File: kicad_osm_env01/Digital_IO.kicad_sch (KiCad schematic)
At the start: 22 parts, among them U18 MIC94073YC6, U20 MIC94073YC6

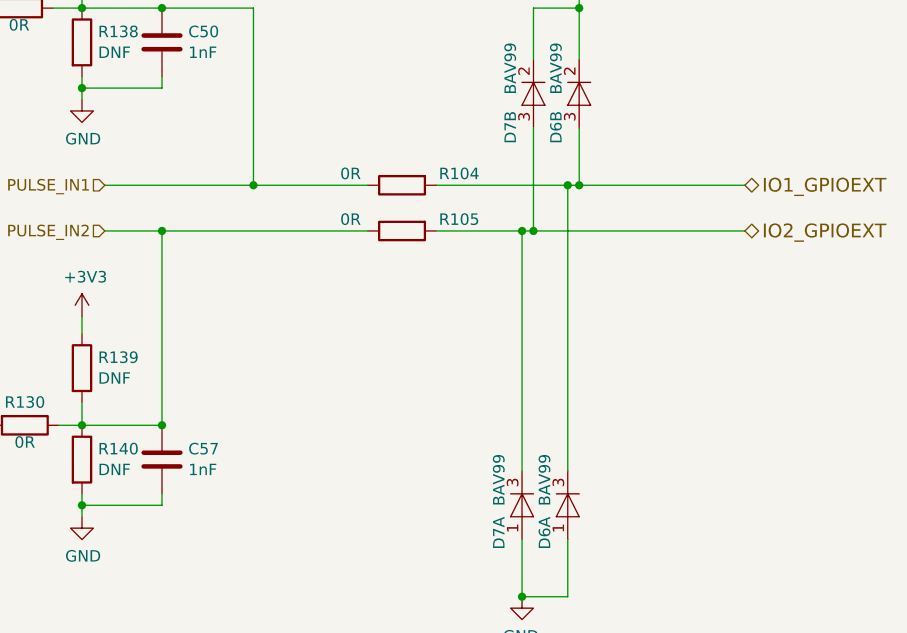
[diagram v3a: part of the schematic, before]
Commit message: updated schematics with 5V ored circuit and new 3v3 regulator
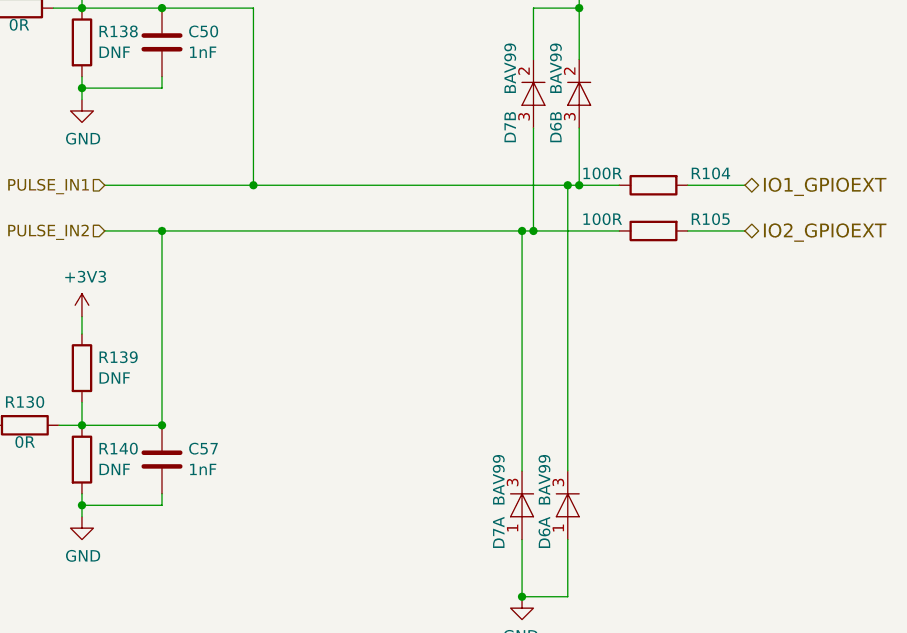
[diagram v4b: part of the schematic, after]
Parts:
- R104, R105: value 0R -> 100R
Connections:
- net IO1_GPIOEXT: no longer D6.3 (A), D6.3 (K)
- net IO2_GPIOEXT: no longer D7.3 (A), D7.3 (K)
- net PULSE_IN1: now also D6.3 (A), D6.3 (K)
- net PULSE_IN2: now also D7.3 (A), D7.3 (K)
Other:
- moved on the sheet: R104, R105
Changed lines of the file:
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@@
     (comment 1 "Part No: 304-010")
   )
+  (junction (at 208.915 85.09) (diameter 0) (color 0 0 0 0)
+  )
   (junction (at 92.71 65.405) (diameter 0) (color 0 0 0 0)
   )
@@
   (junction (at 154.94 120.65) (diameter 0) (color 0 0 0 0)
   )
+  (junction (at 205.105 90.17) (diameter 0) (color 0 0 0 0)
+  )
   (junction (at 203.835 90.17) (diameter 0) (color 0 0 0 0)
   )
@@
   (junction (at 93.345 111.76) (diameter 0) (color 0 0 0 0)
   )
-  (junction (at 205.105 90.17) (diameter 0) (color 0 0 0 0)
-  )
   (junction (at 120.65 148.59) (diameter 0) (color 0 0 0 0)
   )
+  (junction (at 210.185 85.09) (diameter 0) (color 0 0 0 0)
+  )
   (junction (at 154.94 65.405) (diameter 0) (color 0 0 0 0)
   )
@@
   (junction (at 154.94 111.76) (diameter 0) (color 0 0 0 0)
   )
-  (junction (at 208.915 85.09) (diameter 0) (color 0 0 0 0)
-  )
   (junction (at 173.99 85.09) (diameter 0) (color 0 0 0 0)
   )
   (junction (at 98.425 132.08) (diameter 0) (color 0 0 0 0)
   )
-  (junction (at 210.185 85.09) (diameter 0) (color 0 0 0 0)
-  )
   (junction (at 120.015 102.235) (diameter 0) (color 0 0 0 0)
   )
@@
     (stroke (width 0) (type default))
   )
-  (wire (pts (xy 173.99 85.09) (xy 186.69 85.09))
+  (wire (pts (xy 173.99 85.09) (xy 208.915 85.09))
     (stroke (width 0) (type default))
   )
@@
     (stroke (width 0) (type default))
   )
+  (wire (pts (xy 222.25 85.09) (xy 228.6 85.09))
+    (stroke (width 0) (type default))
+  )
   (wire (pts (xy 142.875 111.76) (xy 142.875 122.555))
     (stroke (width 0) (type default))
   )
+  (wire (pts (xy 208.915 85.09) (xy 210.185 85.09))
+    (stroke (width 0) (type default))
+  )
   (wire (pts (xy 151.765 65.405) (xy 154.94 65.405))
     (stroke (width 0) (type default))
@@
     (stroke (width 0) (type default))
   )
-  (wire (pts (xy 208.915 85.09) (xy 194.31 85.09))
-    (stroke (width 0) (type default))
-  )
   (wire (pts (xy 92.71 73.025) (xy 92.71 74.93))
     (stroke (width 0) (type default))
@@
     (stroke (width 0) (type default))
   )
+  (wire (pts (xy 208.915 85.09) (xy 208.915 116.84))
+    (stroke (width 0) (type default))
+  )
   (wire (pts (xy 154.94 65.405) (xy 163.83 65.405))
     (stroke (width 0) (type default))
   )
-  (wire (pts (xy 186.69 90.17) (xy 163.83 90.17))
+  (wire (pts (xy 163.83 90.17) (xy 203.835 90.17))
     (stroke (width 0) (type default))
   )
@@
     (stroke (width 0) (type default))
   )
+  (wire (pts (xy 210.185 85.09) (xy 214.63 85.09))
+    (stroke (width 0) (type default))
+  )
   (wire (pts (xy 97.79 94.615) (xy 97.79 93.345))
     (stroke (width 0) (type default))
   )
-  (wire (pts (xy 210.185 85.09) (xy 208.915 85.09))
-    (stroke (width 0) (type default))
-  )
   (wire (pts (xy 87.63 111.76) (xy 93.345 111.76))
     (stroke (width 0) (type default))
   )
-  (wire (pts (xy 228.6 90.17) (xy 205.105 90.17))
-    (stroke (width 0) (type default))
-  )
   (wire (pts (xy 74.295 111.76) (xy 74.295 110.49))
     (stroke (width 0) (type default))
@@
     (stroke (width 0) (type default))
   )
-  (wire (pts (xy 203.835 90.17) (xy 194.31 90.17))
-    (stroke (width 0) (type default))
-  )
   (wire (pts (xy 173.99 65.405) (xy 173.99 85.09))
     (stroke (width 0) (type default))
@@
     (stroke (width 0) (type default))
   )
-  (wire (pts (xy 208.915 116.84) (xy 208.915 85.09))
-    (stroke (width 0) (type default))
-  )
   (wire (pts (xy 163.83 90.17) (xy 157.48 90.17))
     (stroke (width 0) (type default))
@@
     (stroke (width 0) (type default))
   )
-  (wire (pts (xy 228.6 85.09) (xy 210.185 85.09))
-    (stroke (width 0) (type default))
-  )
   (wire (pts (xy 120.65 148.59) (xy 125.73 148.59))
     (stroke (width 0) (type default))
   )
+  (wire (pts (xy 205.105 90.17) (xy 214.63 90.17))
+    (stroke (width 0) (type default))
+  )
   (wire (pts (xy 80.01 111.76) (xy 74.295 111.76))
     (stroke (width 0) (type default))
@@
   )
   (wire (pts (xy 154.94 111.76) (xy 163.83 111.76))
+    (stroke (width 0) (type default))
+  )
+  (wire (pts (xy 222.25 90.17) (xy 228.6 90.17))
     (stroke (width 0) (type default))
   )
@@
     )
   )
-  (symbol (lib_id "Device:R") (at 190.5 85.09 90) (mirror x) (unit 1)
-    (in_bom yes) (on_board yes) (dnp no)
-    (property "Reference" "R104" (at 196.85 83.82 90)
+  (symbol (lib_id "Device:R") (at 218.44 85.09 90) (mirror x) (unit 1)
+    (in_bom yes) (on_board yes) (dnp no)
+    (property "Reference" "R104" (at 224.79 83.82 90)
       (effects (font (size 1.27 1.27)))
     )
-    (property "Value" "0R" (at 184.785 83.82 90)
+    (property "Value" "100R" (at 212.725 83.82 90)
       (effects (font (size 1.27 1.27)))
     )
-    (property "Footprint" "Resistor_SMD:R_0603_1608Metric" (at 190.5 83.312 90)
-      (effects (font (size 1.27 1.27)) hide)
-    )
-    (property "Datasheet" "" (at 190.5 85.09 0)
+    (property "Footprint" "Resistor_SMD:R_0603_1608Metric" (at 218.44 83.312 90)
+      (effects (font (size 1.27 1.27)) hide)
+    )
+    (property "Datasheet" "" (at 218.44 85.09 0)
       (effects (font (size 1.27 1.27)) hide)
     )
@@
     )
   )
-  (symbol (lib_id "Device:R") (at 190.5 90.17 90) (mirror x) (unit 1)
-    (in_bom yes) (on_board yes) (dnp no)
-    (property "Reference" "R105" (at 196.85 88.9 90)
+  (symbol (lib_id "Device:R") (at 218.44 90.17 90) (mirror x) (unit 1)
+    (in_bom yes) (on_board yes) (dnp no)
+    (property "Reference" "R105" (at 224.79 88.9 90)
       (effects (font (size 1.27 1.27)))
     )
-    (property "Value" "0R" (at 184.785 88.9 90)
+    (property "Value" "100R" (at 212.725 88.9 90)
       (effects (font (size 1.27 1.27)))
     )
-    (property "Footprint" "Resistor_SMD:R_0603_1608Metric" (at 190.5 88.392 90)
-      (effects (font (size 1.27 1.27)) hide)
-    )
-    (property "Datasheet" "" (at 190.5 90.17 0)
-      (effects (font (size 1.27 1.27)) hide)
-    )
+    (property "Footprint" "Resistor_SMD:R_0603_1608Metric" (at 218.44 88.392 90)
+      (effects (font (size 1.27 1.27)) hide)
+    )
+    (property "Datasheet" "" (at 218.44 90.17 0)
+      (effects (font (size 1.27 1.27)) hide)
+    )

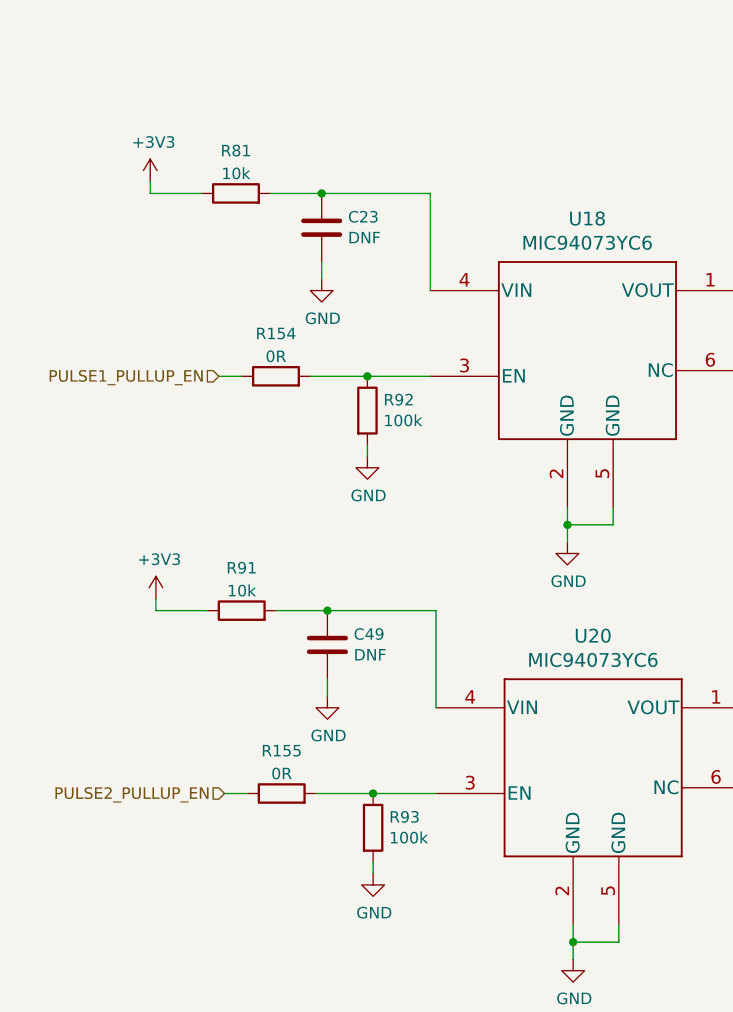
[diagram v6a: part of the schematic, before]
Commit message: assigned all footprints
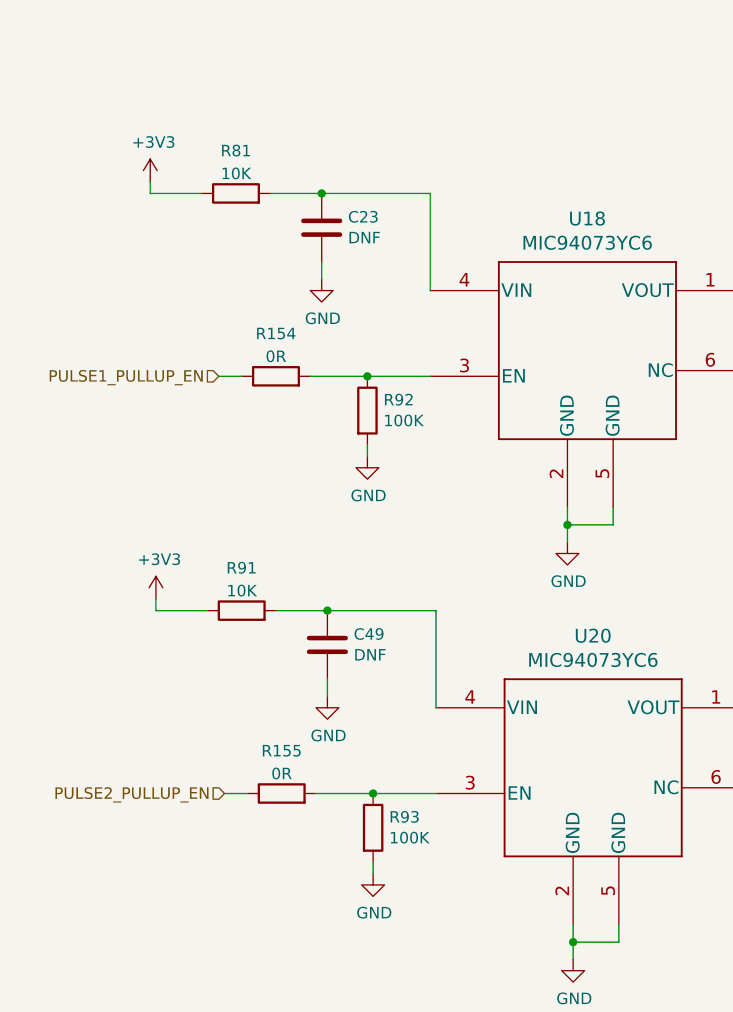
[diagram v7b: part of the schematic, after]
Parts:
- R130, R137, R138, R139, R140, R154, R155, R94: footprint Resistor_SMD:R_0603_1608Metric -> Resistor_SMD:R_0402_1005Metric
- R81, R91: value 10k -> 10K; footprint Resistor_SMD:R_0603_1608Metric -> Resistor_SMD:R_0402_1005Metric
- R92, R93: value 100k -> 100K; footprint Resistor_SMD:R_0603_1608Metric -> Resistor_SMD:R_0402_1005Metric
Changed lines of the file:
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@@
   (title_block
     (title "Open Smart Monitor")
-    (date "2022-09-26")
-    (rev "C")
+    (date "2023-09-29")
+    (rev "C.2")
     (company "Devtank LTD")
     (comment 1 "Part No: 304-010")
@@
       (effects (font (size 1.27 1.27)))
     )
-    (property "Value" "10k" (at 83.185 63.2261 90)
-      (effects (font (size 1.27 1.27)))
-    )
-    (property "Footprint" "Resistor_SMD:R_0603_1608Metric" (at 83.185 67.183 90)
-      (effects (font (size 1.27 1.27)) hide)
-    )
-    (property "Datasheet" "~" (at 83.185 65.405 0)
+    (property "Value" "10K" (at 83.185 63.2261 90)
+      (effects (font (size 1.27 1.27)))
+    )
+    (property "Footprint" "Resistor_SMD:R_0402_1005Metric" (at 83.185 67.183 90)
+      (effects (font (size 1.27 1.27)) hide)
+    )
+    (property "Datasheet" "" (at 83.185 65.405 0)
       (effects (font (size 1.27 1.27)) hide)
     )
@@
       (effects (font (size 1.27 1.27)) (justify left))
     )
-    (property "Footprint" "Resistor_SMD:R_0603_1608Metric" (at 153.162 105.41 90)
+    (property "Footprint" "Resistor_SMD:R_0402_1005Metric" (at 153.162 105.41 90)
       (effects (font (size 1.27 1.27)) hide)
     )
@@
       (effects (font (size 1.27 1.27)))
     )
-    (property "Footprint" "Resistor_SMD:R_0603_1608Metric" (at 87.63 87.503 90)
-      (effects (font (size 1.27 1.27)) hide)
-    )
-    (property "Datasheet" "~" (at 87.63 85.725 0)
+    (property "Footprint" "Resistor_SMD:R_0402_1005Metric" (at 87.63 87.503 90)
+      (effects (font (size 1.27 1.27)) hide)
+    )
+    (property "Datasheet" "" (at 87.63 85.725 0)
       (effects (font (size 1.27 1.27)) hide)
     )
@@
       (effects (font (size 1.27 1.27)))
     )
-    (property "Footprint" "Resistor_SMD:R_0603_1608Metric" (at 148.59 109.982 90)
+    (property "Footprint" "Resistor_SMD:R_0402_1005Metric" (at 148.59 109.982 90)
       (effects (font (size 1.27 1.27)) hide)
     )
@@
       (effects (font (size 1.27 1.27)) (justify left))
     )
-    (property "Footprint" "Resistor_SMD:R_0603_1608Metric" (at 153.162 58.42 90)
+    (property "Footprint" "Resistor_SMD:R_0402_1005Metric" (at 153.162 58.42 90)
       (effects (font (size 1.27 1.27)) hide)
     )
@@
       (effects (font (size 1.27 1.27)))
     )
-    (property "Footprint" "Resistor_SMD:R_0603_1608Metric" (at 88.265 133.858 90)
-      (effects (font (size 1.27 1.27)) hide)
-    )
-    (property "Datasheet" "~" (at 88.265 132.08 0)
+    (property "Footprint" "Resistor_SMD:R_0402_1005Metric" (at 88.265 133.858 90)
+      (effects (font (size 1.27 1.27)) hide)
+    )
+    (property "Datasheet" "" (at 88.265 132.08 0)
       (effects (font (size 1.27 1.27)) hide)
     )
@@
       (effects (font (size 1.27 1.27)) (justify left))
     )
-    (property "Footprint" "Resistor_SMD:R_0603_1608Metric" (at 153.162 115.57 90)
+    (property "Footprint" "Resistor_SMD:R_0402_1005Metric" (at 153.162 115.57 90)
       (effects (font (size 1.27 1.27)) hide)
     )
@@
       (effects (font (size 1.27 1.27)))
     )
-    (property "Footprint" "Resistor_SMD:R_0603_1608Metric" (at 147.955 63.627 90)
+    (property "Footprint" "Resistor_SMD:R_0402_1005Metric" (at 147.955 63.627 90)
       (effects (font (size 1.27 1.27)) hide)
     )
@@
       (effects (font (size 1.27 1.27)) (justify left))
     )
-    (property "Value" "100k" (at 99.568 90.678 0)
-      (effects (font (size 1.27 1.27)) (justify left))
-    )
-    (property "Footprint" "Resistor_SMD:R_0603_1608Metric" (at 96.012 89.535 90)
+    (property "Value" "100K" (at 99.568 90.678 0)
+      (effects (font (size 1.27 1.27)) (justify left))
+    )
+    (property "Footprint" "Resistor_SMD:R_0402_1005Metric" (at 96.012 89.535 90)
       (effects (font (size 1.27 1.27)) hide)
     )
@@
       (effects (font (size 1.27 1.27)) (justify left))
     )
-    (property "Value" "100k" (at 100.203 137.033 0)
-      (effects (font (size 1.27 1.27)) (justify left))
-    )
-    (property "Footprint" "Resistor_SMD:R_0603_1608Metric" (at 96.647 135.89 90)
+    (property "Value" "100K" (at 100.203 137.033 0)
+      (effects (font (size 1.27 1.27)) (justify left))
+    )
+    (property "Footprint" "Resistor_SMD:R_0402_1005Metric" (at 96.647 135.89 90)
       (effects (font (size 1.27 1.27)) hide)
     )
@@
       (effects (font (size 1.27 1.27)))
     )
-    (property "Value" "10k" (at 83.82 109.5811 90)
-      (effects (font (size 1.27 1.27)))
-    )
-    (property "Footprint" "Resistor_SMD:R_0603_1608Metric" (at 83.82 113.538 90)
-      (effects (font (size 1.27 1.27)) hide)
-    )
-    (property "Datasheet" "~" (at 83.82 111.76 0)
+    (property "Value" "10K" (at 83.82 109.5811 90)
+      (effects (font (size 1.27 1.27)))
+    )
+    (property "Footprint" "Resistor_SMD:R_0402_1005Metric" (at 83.82 113.538 90)
+      (effects (font (size 1.27 1.27)) hide)
+    )
+    (property "Datasheet" "" (at 83.82 111.76 0)
       (effects (font (size 1.27 1.27)) hide)
     )
@@
       (effects (font (size 1.27 1.27)) (justify left))
     )
-    (property "Footprint" "Resistor_SMD:R_0603_1608Metric" (at 153.162 69.215 90)
-      (effects (font (size 1.27 1.27)) hide)
-    )
+    (property "Footprint" "Resistor_SMD:R_0402_1005Metric" (at 153.162 69.215 90)
+      (effects (font (size 1.27 1.27)) hide)
+    )
